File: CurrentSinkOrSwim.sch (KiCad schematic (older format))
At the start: 1 part

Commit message: Adding preliminary values to the componenets
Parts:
- removed U?: AD390JD, symbol AD390JD
- added C? (x2): C, symbol C
- added P?: CONN_01X02, symbol CONN_01X02
- added Q?: Q_NMOS_DGS, symbol Q_NMOS_DGS
- added R? (x2): R, symbol R
- added RV?: POT, symbol POT
- added U? (x2): LMV358, symbol LMV358
- added U?: TC1016, symbol TC1016
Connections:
- net labels added: GND
- wire segments 0 -> 28
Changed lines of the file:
@@
 LIBS:contrib
 LIBS:valves
+LIBS:CurrentSinkOrSwim
+LIBS:CurrentSinkOrSwim-cache
 EELAYER 25 0
 EELAYER END
@@
 $EndDescr
 $Comp
-L AD390JD U?
-U 1 1 5647D5D9
-P 4700 3300
-F 0 "U?" H 4150 4500 50  0000 L CNN
-F 1 "AD390JD" H 5050 4500 50  0000 L CNN
-F 2 "" H 4700 3400 50  0000 C CNN
-F 3 "" H 4700 3400 50  0000 C CNN
-	1    4700 3300
-	1    0    0    -1
-$EndComp
+L R R?
+U 1 1 564915F9
+P 6050 5150
+F 0 "R?" V 6130 5150 50  0000 C CNN
+F 1 "R" V 6050 5150 50  0000 C CNN
+F 2 "" V 5980 5150 30  0000 C CNN
+F 3 "" H 6050 5150 30  0000 C CNN
+	1    6050 5150
+	1    0    0    -1
+$EndComp
+$Comp
+L GND #PWR?
+U 1 1 5649165C
+P 6050 5650
+F 0 "#PWR?" H 6050 5400 50  0001 C CNN
+F 1 "GND" H 6050 5500 50  0000 C CNN
+F 2 "" H 6050 5650 60  0000 C CNN
+F 3 "" H 6050 5650 60  0000 C CNN
+	1    6050 5650
+	1    0    0    -1
+$EndComp
+$Comp
+L LMV358 U?
+U 1 1 56664EC8
+P 4750 4050
+F 0 "U?" H 4700 4250 60  0000 L CNN
+F 1 "LMV358" H 4700 3800 60  0000 L CNN
+F 2 "" H 4750 4050 60  0000 C CNN
+F 3 "" H 4750 4050 60  0000 C CNN
+	1    4750 4050
+	1    0    0    -1
+$EndComp
+$Comp
+L Q_NMOS_DGS Q?
+U 1 1 56664F49
+P 5950 4050
+F 0 "Q?" H 6250 4100 50  0000 R CNN
+F 1 "Q_NMOS_DGS" H 6600 4000 50  0000 R CNN
+F 2 "" H 6150 4150 50  0000 C CNN
+F 3 "" H 5950 4050 50  0000 C CNN
+	1    5950 4050
+	1    0    0    -1
+$EndComp
+$Comp
+L R R?
+U 1 1 566650C9
+P 2750 4550
+F 0 "R?" V 2830 4550 50  0000 C CNN
+F 1 "R" V 2750 4550 50  0000 C CNN
+F 2 "" V 2680 4550 50  0000 C CNN
+F 3 "" H 2750 4550 50  0000 C CNN
+	1    2750 4550
+	1    0    0    -1
+$EndComp
+Wire Wire Line
+	6050 5300 6050 5650
+Wire Wire Line
+	6050 4250 6050 5000
+$Comp
+L GND #PWR?
+U 1 1 566651F5
+P 4650 4550
+F 0 "#PWR?" H 4650 4300 50  0001 C CNN
+F 1 "GND" H 4650 4400 50  0000 C CNN
+F 2 "" H 4650 4550 60  0000 C CNN
+F 3 "" H 4650 4550 60  0000 C CNN
+	1    4650 4550
+	1    0    0    -1
+$EndComp
+Wire Wire Line
+	4650 4550 4650 4450
+Wire Wire Line
+	2750 3950 2750 4400
+Wire Wire Line
+	5600 4800 4050 4800
+Wire Wire Line
+	4050 4800 4050 4150
+Wire Wire Line
+	4050 4150 4250 4150
+Connection ~ 6050 4400
+Wire Wire Line
+	5750 4050 5250 4050
+Wire Wire Line
+	5600 4800 5600 4400
+Wire Wire Line
+	5600 4400 6050 4400
+Wire Wire Line
+	4650 3050 4650 3650
+Wire Wire Line
+	2750 4700 2750 5500
+Wire Wire Line
+	2750 5500 6050 5500
+Connection ~ 6050 5500
+$Comp
+L TC1016 U?
+U 1 1 566654FD
+P 5350 3100
+F 0 "U?" H 5500 2904 50  0000 C CNN
+F 1 "TC1016" H 5350 3300 50  0000 C CNN
+F 2 "" H 5350 3100 50  0000 C CNN
+F 3 "" H 5350 3100 50  0000 C CNN
+	1    5350 3100
+	-1   0    0    -1
+$EndComp
+Wire Wire Line
+	6050 3050 6050 3850
+Connection ~ 4650 3050
+Wire Wire Line
+	5750 3050 6600 3050
+$Comp
+L GND #PWR?
+U 1 1 566659A2
+P 5350 3600
+F 0 "#PWR?" H 5350 3350 50  0001 C CNN
+F 1 "GND" H 5350 3450 50  0000 C CNN
+F 2 "" H 5350 3600 60  0000 C CNN
+F 3 "" H 5350 3600 60  0000 C CNN
+	1    5350 3600
+	1    0    0    -1
+$EndComp
+$Comp
+L C C?
+U 1 1 566659DC
+P 4850 3300
+F 0 "C?" H 4875 3400 50  0000 L CNN
+F 1 "C" H 4875 3200 50  0000 L CNN
+F 2 "" H 4888 3150 50  0000 C CNN
+F 3 "" H 4850 3300 50  0000 C CNN
+	1    4850 3300
+	1    0    0    -1
+$EndComp
+$Comp
+L C C?
+U 1 1 56665A11
+P 5800 3300
+F 0 "C?" H 5825 3400 50  0000 L CNN
+F 1 "C" H 5825 3200 50  0000 L CNN
+F 2 "" H 5838 3150 50  0000 C CNN
+F 3 "" H 5800 3300 50  0000 C CNN
+	1    5800 3300
+	1    0    0    -1
+$EndComp
+Wire Wire Line
+	4850 3150 4850 3050
+Connection ~ 4850 3050
+Wire Wire Line
+	5800 3150 5800 3050
+Connection ~ 5800 3050
+Wire Wire Line
+	4850 3450 4850 3500
+Wire Wire Line
+	4850 3500 5350 3500
+Wire Wire Line
+	5350 3350 5350 3600
+Connection ~ 5350 3500
+Wire Wire Line
+	5800 3450 5350 3450
+Connection ~ 5350 3450
+Wire Wire Line
+	4250 3950 3600 3950
+Wire Wire Line
+	3600 3950 3600 4150
+Wire Wire Line
+	3600 4150 2750 4150
+Connection ~ 2750 4150
+$Comp
+L POT RV?
+U 1 1 56665D1E
+P 2750 3700
+F 0 "RV?" H 2750 3600 50  0000 C CNN
+F 1 "POT" H 2750 3700 50  0000 C CNN
+F 2 "" H 2750 3700 50  0000 C CNN
+F 3 "" H 2750 3700 50  0000 C CNN
+	1    2750 3700
+	0    1    1    0
+$EndComp
+Wire Wire Line
+	2900 3700 2900 3050
+Wire Wire Line
+	2900 3050 4950 3050
+$Comp
+L CONN_01X02 P?
+U 1 1 56665F04
+P 6800 3100
+F 0 "P?" H 6800 3250 50  0000 C CNN
+F 1 "CONN_01X02" V 6900 3100 50  0000 C CNN
+F 2 "" H 6800 3100 50  0000 C CNN
+F 3 "" H 6800 3100 50  0000 C CNN
+	1    6800 3100
+	1    0    0    -1
+$EndComp
+Connection ~ 6050 3050
+$Comp
+L GND #PWR?
+U 1 1 56665FA8
+P 6400 3550
+F 0 "#PWR?" H 6400 3300 50  0001 C CNN
+F 1 "GND" H 6400 3400 50  0000 C CNN
+F 2 "" H 6400 3550 60  0000 C CNN
+F 3 "" H 6400 3550 60  0000 C CNN
+	1    6400 3550
+	1    0    0    -1
+$EndComp
+Wire Wire Line
+	6600 3150 6400 3150
+Wire Wire Line
+	6400 3150 6400 3550
+$Comp
+L LMV358 U?
+U 2 1 56666017
+P 7650 5000
+F 0 "U?" H 7600 5200 60  0000 L CNN
+F 1 "LMV358" H 7600 4750 60  0000 L CNN
+F 2 "" H 7650 5000 60  0000 C CNN
+F 3 "" H 7650 5000 60  0000 C CNN
+	2    7650 5000
+	1    0    0    -1
+$EndComp

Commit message: Added Current Sink or Swim Schematic Hierarchy Sheet
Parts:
- removed C? (x2): C, symbol C
- removed Q?: Q_NMOS_DGS, symbol Q_NMOS_DGS
- removed R? (x2): R, symbol R
- removed RV?: POT, symbol POT
- removed U? (x2): LMV358, symbol LMV358
- removed U?: TC1016, symbol TC1016
- added P?: CONN_01X03, symbol CONN_01X03
- added P?: CONN_01X02, symbol CONN_01X02
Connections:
- wire segments 28 -> 17
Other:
- note added: "Battery Pack\n"
- note added: "Current sink input"
- moved on the sheet: P?

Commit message: Annotated sheets
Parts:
- gave numbers to parts that had none: 3
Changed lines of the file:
@@
 $EndDescr
 $Comp
-L CONN_01X02 P?
+L CONN_01X02 P103
 U 1 1 56665F04
 P 7650 1450
-F 0 "P?" H 7650 1600 50  0000 C CNN
+F 0 "P103" H 7650 1600 50  0000 C CNN
 F 1 "CONN_01X02" V 7750 1450 50  0000 C CNN
 F 2 "" H 7650 1450 50  0000 C CNN
@@
 $EndComp
 $Comp
-L CONN_01X03 P?
+L CONN_01X03 P102
 U 1 1 56A5A7D2
 P 5950 1050
-F 0 "P?" H 5950 1250 50  0000 C CNN
+F 0 "P102" H 5950 1250 50  0000 C CNN
 F 1 "CONN_01X03" V 6050 1050 50  0000 C CNN
 F 2 "" H 5950 1050 50  0000 C CNN
@@
 $EndComp
 Wire Wire Line
-	7450 6650 7450 1500
+	7450 1500 7450 6200
 Connection ~ 6050 1400
 Wire Wire Line
@@
 	2800 1250 5850 1250
 $Comp
-L CONN_01X02 P?
+L CONN_01X02 P101
 U 1 1 56A5AB45
 P 2600 1300
-F 0 "P?" H 2600 1450 50  0000 C CNN
+F 0 "P101" H 2600 1450 50  0000 C CNN
 F 1 "CONN_01X02" V 2700 1300 50  0000 C CNN
 F 2 "" H 2600 1300 50  0000 C CNN
@@
 $EndComp
 Wire Wire Line
-	7400 6650 7400 7200
+	7400 6200 7400 7200
 $Comp
-L GND #PWR?
+L GND #PWR102
 U 1 1 56A5ACAF
 P 7400 7200
-F 0 "#PWR?" H 7400 6950 50  0001 C CNN
+F 0 "#PWR102" H 7400 6950 50  0001 C CNN
 F 1 "GND" H 7400 7050 50  0000 C CNN
 F 2 "" H 7400 7200 60  0000 C CNN
@@
 F2 "Vcontrol" O L 4350 6200 60
 F3 "Current_Sink+" I R 5750 6000 60
-F4 "Current_Sink-" I R 5750 6650 60
+F4 "Current_Sink-" I R 5750 6250 60
 $EndSheet
 $Sheet
@@
 Connection ~ 7050 4200
 Wire Wire Line
-	5750 6650 7450 6650
+	7450 6200 7400 6200
 Connection ~ 7450 4550
 Wire Wire Line
 	3250 1350 3250 2050
 $Comp
-L GND #PWR?
+L GND #PWR101
 U 1 1 56A61040
 P 3250 2050
-F 0 "#PWR?" H 3250 1800 50  0001 C CNN
+F 0 "#PWR101" H 3250 1800 50  0001 C CNN
 F 1 "GND" H 3250 1900 50  0000 C CNN
 F 2 "" H 3250 2050 60  0000 C CNN
@@
 Wire Wire Line
 	3250 1350 2800 1350
-Connection ~ 7400 6650
+Connection ~ 7400 6200
 Wire Wire Line
 	4400 4650 3900 4650
@@
 Wire Wire Line
 	3900 6200 4350 6200
+Wire Wire Line
+	5750 6250 7400 6250
+Connection ~ 7400 6250
 $EndSCHEMATC

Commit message: Updated BOM
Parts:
- P101, P103: footprint (none) -> Connect:AK300-2; MPN (none) -> OSTTCD22162
- P102: footprint (none) -> Pin_Headers:Pin_Header_Straight_1x03
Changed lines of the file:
@@
 EESchema Schematic File Version 2
+LIBS:CurrentSinkOrSwim-rescue
 LIBS:power
 LIBS:device
@@
 F 0 "P103" H 7650 1600 50  0000 C CNN
 F 1 "CONN_01X02" V 7750 1450 50  0000 C CNN
-F 2 "" H 7650 1450 50  0000 C CNN
+F 2 "Connect:AK300-2" H 7650 1450 50  0001 C CNN
 F 3 "" H 7650 1450 50  0000 C CNN
+F 4 "OSTTCD22162" H 7650 1450 60  0001 C CNN "MPN"
 	1    7650 1450
 	1    0    0    -1
@@
 F 0 "P102" H 5950 1250 50  0000 C CNN
 F 1 "CONN_01X03" V 6050 1050 50  0000 C CNN
-F 2 "" H 5950 1050 50  0000 C CNN
+F 2 "Pin_Headers:Pin_Header_Straight_1x03" H 5950 1050 50  0001 C CNN
 F 3 "" H 5950 1050 50  0000 C CNN
 	1    5950 1050
@@
 F 0 "P101" H 2600 1450 50  0000 C CNN
 F 1 "CONN_01X02" V 2700 1300 50  0000 C CNN
-F 2 "" H 2600 1300 50  0000 C CNN
+F 2 "Connect:AK300-2" H 2600 1300 50  0001 C CNN
 F 3 "" H 2600 1300 50  0000 C CNN
+F 4 "OSTTCD22162" H 2600 1300 60  0001 C CNN "MPN"
 	1    2600 1300
 	-1   0    0    1
@@
 	7400 6200 7400 7200
 $Comp
-L GND #PWR102
+L GND #PWR01
 U 1 1 56A5ACAF
 P 7400 7200
-F 0 "#PWR102" H 7400 6950 50  0001 C CNN
+F 0 "#PWR01" H 7400 6950 50  0001 C CNN
 F 1 "GND" H 7400 7050 50  0000 C CNN
 F 2 "" H 7400 7200 60  0000 C CNN
@@
 	3250 1350 3250 2050
 $Comp
-L GND #PWR101
+L GND #PWR02
 U 1 1 56A61040
 P 3250 2050
-F 0 "#PWR101" H 3250 1800 50  0001 C CNN
+F 0 "#PWR02" H 3250 1800 50  0001 C CNN
 F 1 "GND" H 3250 1900 50  0000 C CNN
 F 2 "" H 3250 2050 60  0000 C CNN

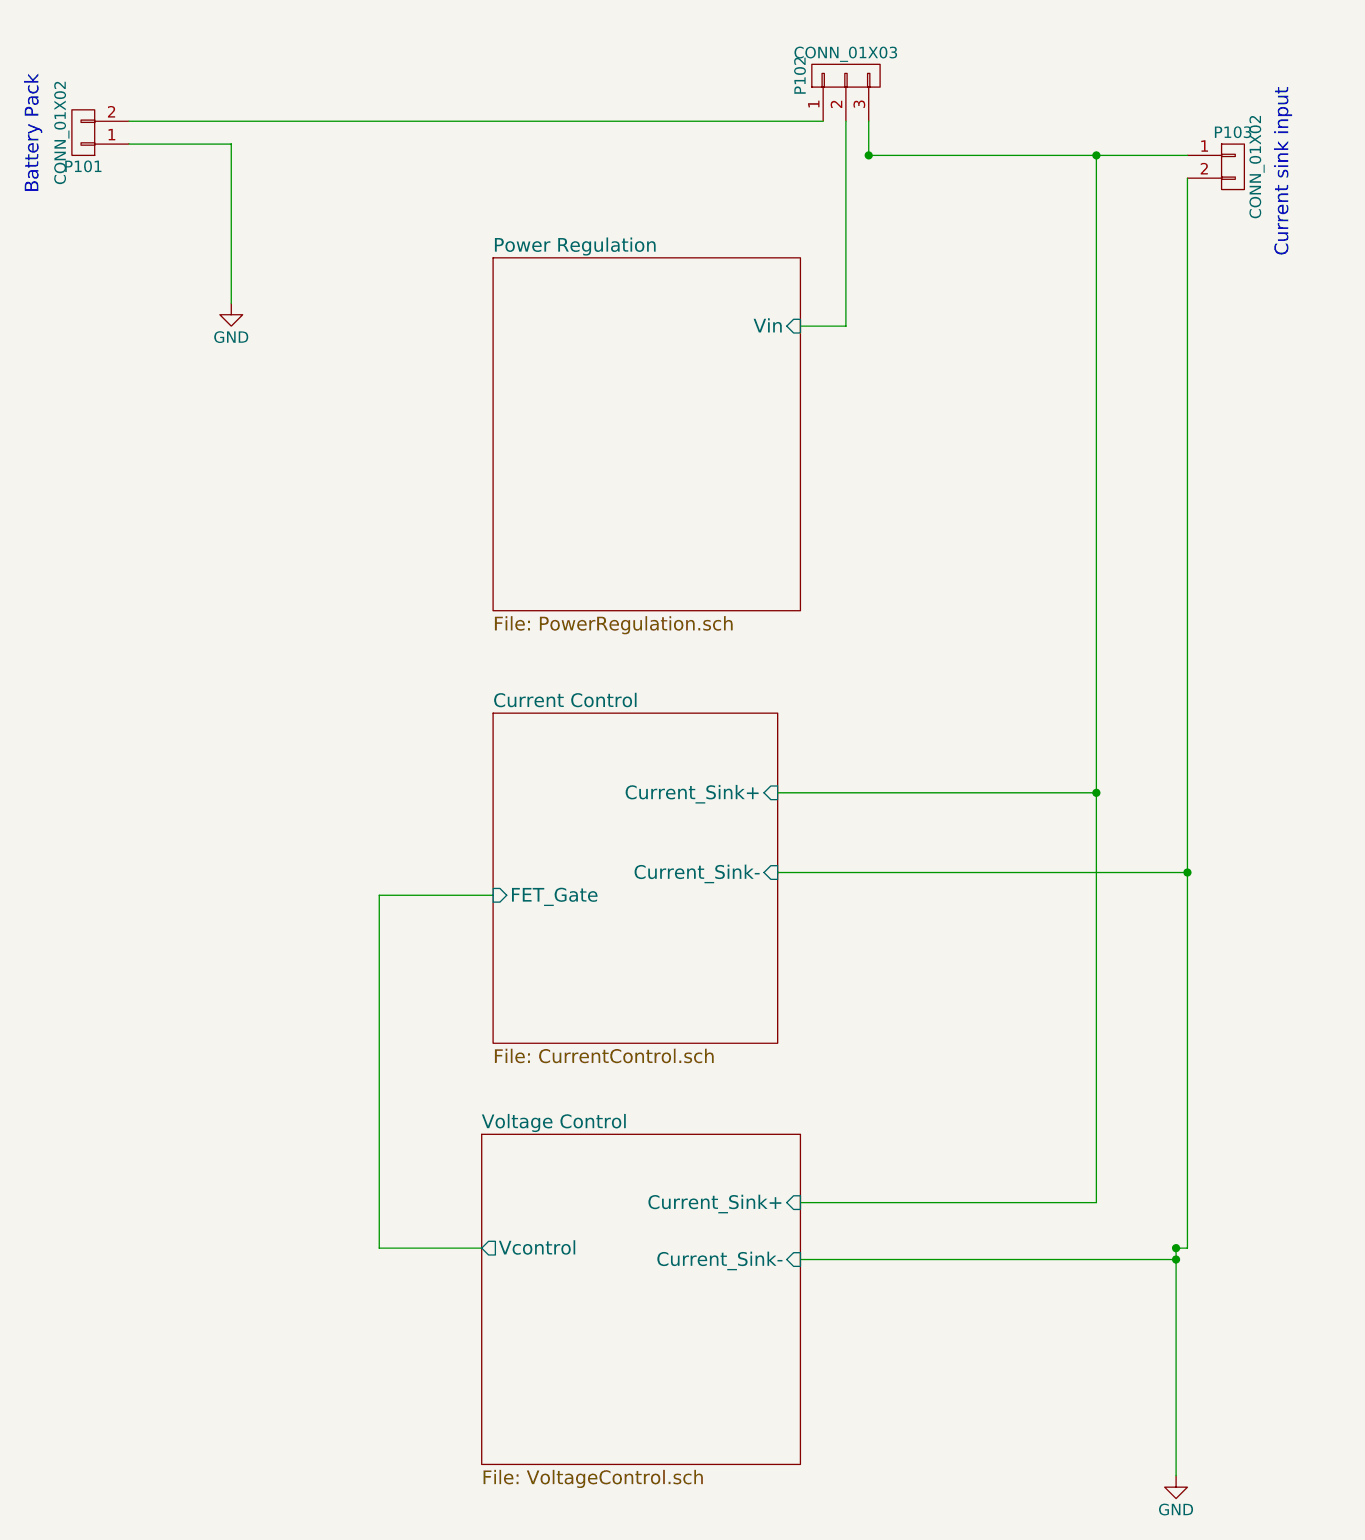
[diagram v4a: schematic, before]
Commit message: This is the version of the file that has been submitted to OSH park
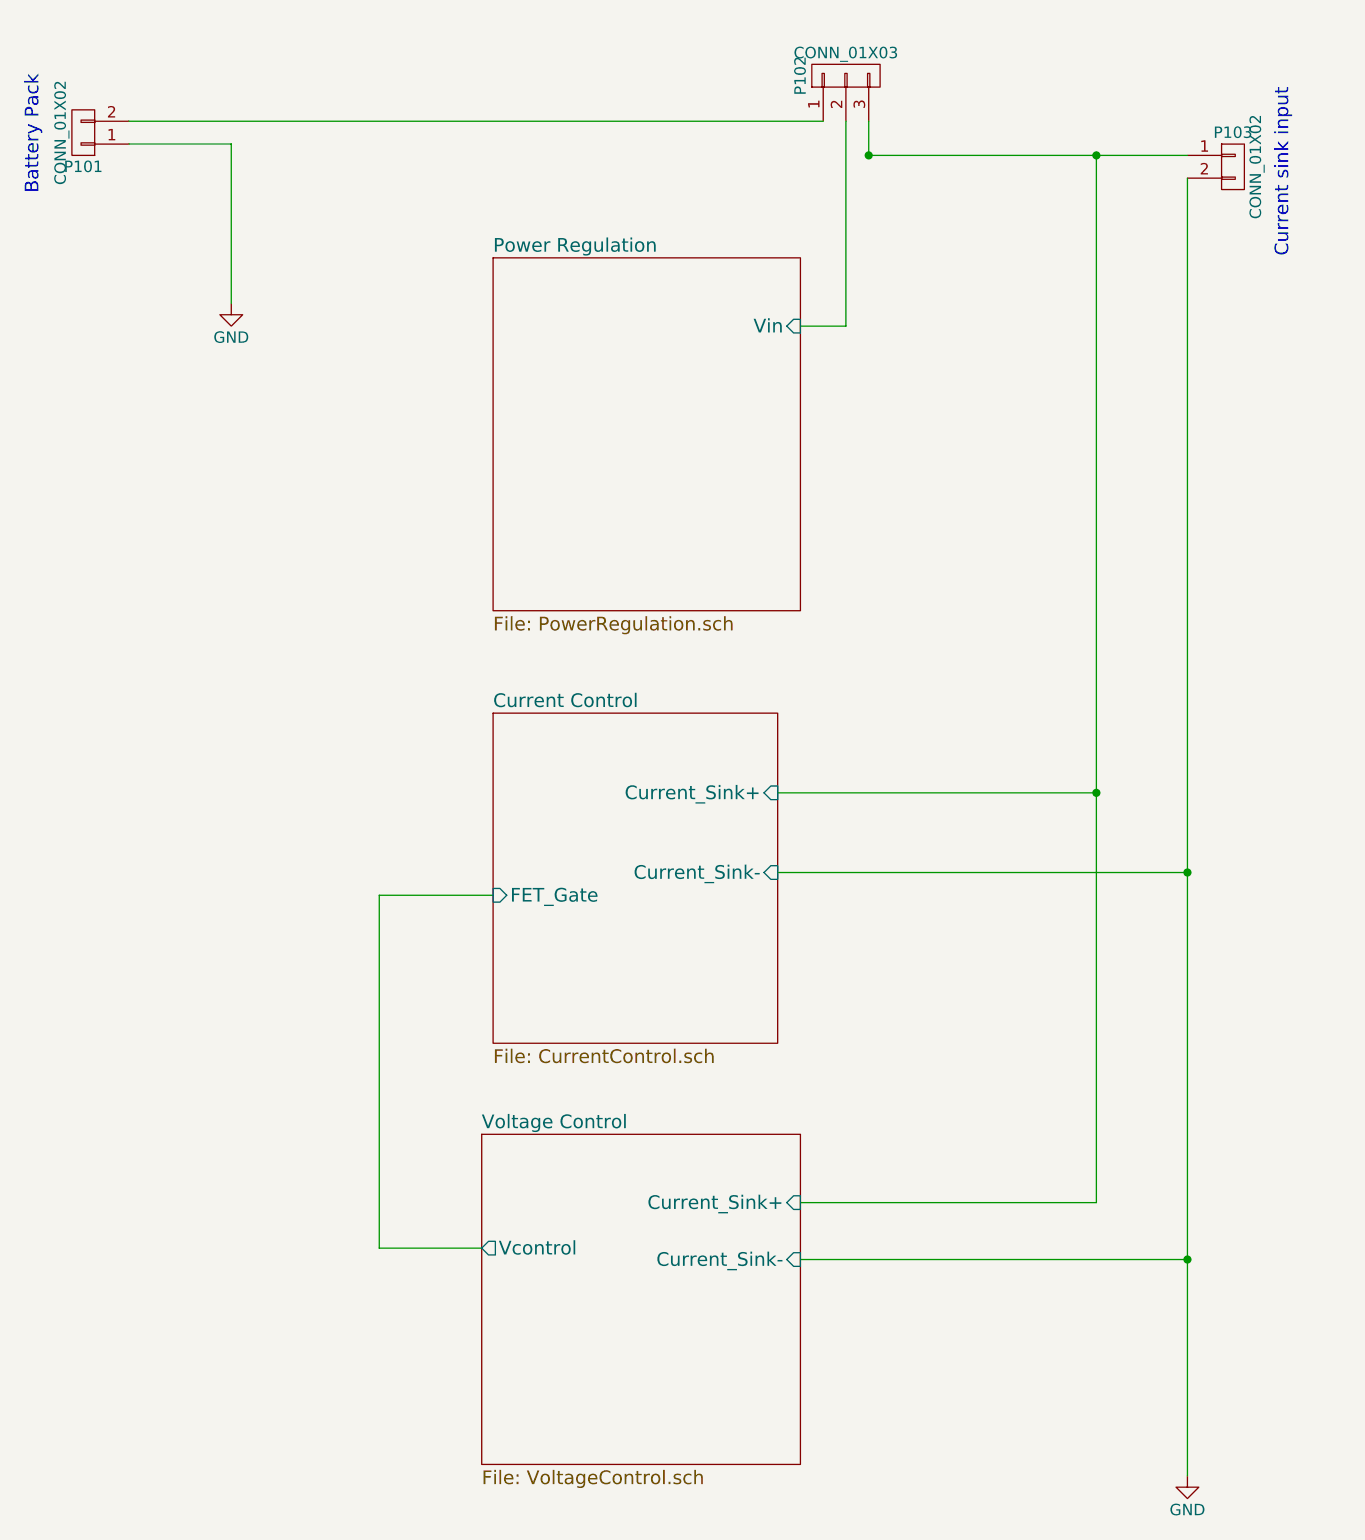
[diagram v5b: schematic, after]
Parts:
- P101, P103: MPN OSTTCD22162 -> OSTTC022162
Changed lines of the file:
@@
 F 2 "Connect:AK300-2" H 7650 1450 50  0001 C CNN
 F 3 "" H 7650 1450 50  0000 C CNN
-F 4 "OSTTCD22162" H 7650 1450 60  0001 C CNN "MPN"
+F 4 "OSTTC022162" H 7650 1450 60  0001 C CNN "MPN"
 	1    7650 1450
 	1    0    0    -1
@@
 $EndComp
 Wire Wire Line
-	7450 1500 7450 6200
+	7450 1500 7450 7200
 Connection ~ 6050 1400
 Wire Wire Line
@@
 F 2 "Connect:AK300-2" H 2600 1300 50  0001 C CNN
 F 3 "" H 2600 1300 50  0000 C CNN
-F 4 "OSTTCD22162" H 2600 1300 60  0001 C CNN "MPN"
+F 4 "OSTTC022162" H 2600 1300 60  0001 C CNN "MPN"
 	1    2600 1300
 	-1   0    0    1
 $EndComp
-Wire Wire Line
-	7400 6200 7400 7200
 $Comp
 L GND #PWR01
 U 1 1 56A5ACAF
-P 7400 7200
-F 0 "#PWR01" H 7400 6950 50  0001 C CNN
-F 1 "GND" H 7400 7050 50  0000 C CNN
-F 2 "" H 7400 7200 60  0000 C CNN
-F 3 "" H 7400 7200 60  0000 C CNN
-	1    7400 7200
+P 7450 7200
+F 0 "#PWR01" H 7450 6950 50  0001 C CNN
+F 1 "GND" H 7450 7050 50  0000 C CNN
+F 2 "" H 7450 7200 60  0000 C CNN
+F 3 "" H 7450 7200 60  0000 C CNN
+	1    7450 7200
 	1    0    0    -1
 $EndComp
@@
 Connection ~ 7050 4200
 Wire Wire Line
-	7450 6200 7400 6200
+	7450 6200 7450 6200
 Connection ~ 7450 4550
 Wire Wire Line
@@
 Wire Wire Line
 	3250 1350 2800 1350
-Connection ~ 7400 6200
 Wire Wire Line
 	4400 4650 3900 4650
@@
 	3900 6200 4350 6200
 Wire Wire Line
-	5750 6250 7400 6250
-Connection ~ 7400 6250
+	5750 6250 7450 6250
+Connection ~ 7450 6250
 $EndSCHEMATC
